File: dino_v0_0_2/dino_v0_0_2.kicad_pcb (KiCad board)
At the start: 4 copper layers, 298.9 x 270 mm, 207 parts, among them J1 DINO_BUS_SOCKET, J10 PS_ON, J11 Conn_01x08_Socket, J2 DINO_BUS_SOCKET, J3 DINO_BUS_SOCKET, J4 DINO_BUS_SOCKET, J5 DINO_BUS_SOCKET, J6 DINO_BUS_SOCKET, J7 DINO_BUS_SOCKET, J8 DINO_BUS_SOCKET, J9 ATX-24, SW2 RESET_BTN, U1 74LS193, U10 74LS02, U11 74LS245, U12 74LS245, U13 74LS245, U14 74LS245, U15 AT28C64B, U16 74LS244N, U17 74LS244N, U18 74LS373, U19 74LS245, U2 74LS193, U20 74LS163, U21 74LS245, U22 74LS02, U23 AT28C64B, U24 AT28C256, U25 74LS245, U26 MCM60256AP, U27 74LS74, U28 74LS138, U29 74LS138, U3 74LS193, U30 74LS138, U31 74LS373, U32 74LS373, U33 74LS373, U34 74LS373, U35 74LS373, U36 7400, U37 74LS04, U38 74F382N, U39 74LS00, U4 74LS193, U40 74F382N, U41 74LS245, U42 74LS245, U43 74LS245, U44 74LS245, U45 74LS373, U46 74LS373, U47 74LS373, U48 74LS157, U49 74LS273, U5 74LS08, U50 74LS02, U51 7400, U52 74LS02, U53 74LS08, U54 74LS245, U55 74LS373, U56 74LS14, U57 74LS02, U58 74LS373, U59 74LS245, U6 74LS163, U60 74LS02, U61 74LS02, U62 74LS02, U63 74LS169, U64 74LS169, U65 74LS169, U66 74LS169, U67 74LS245, U68 74LS245, U69 74LS08, U7 74LS138, U70 74LS138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

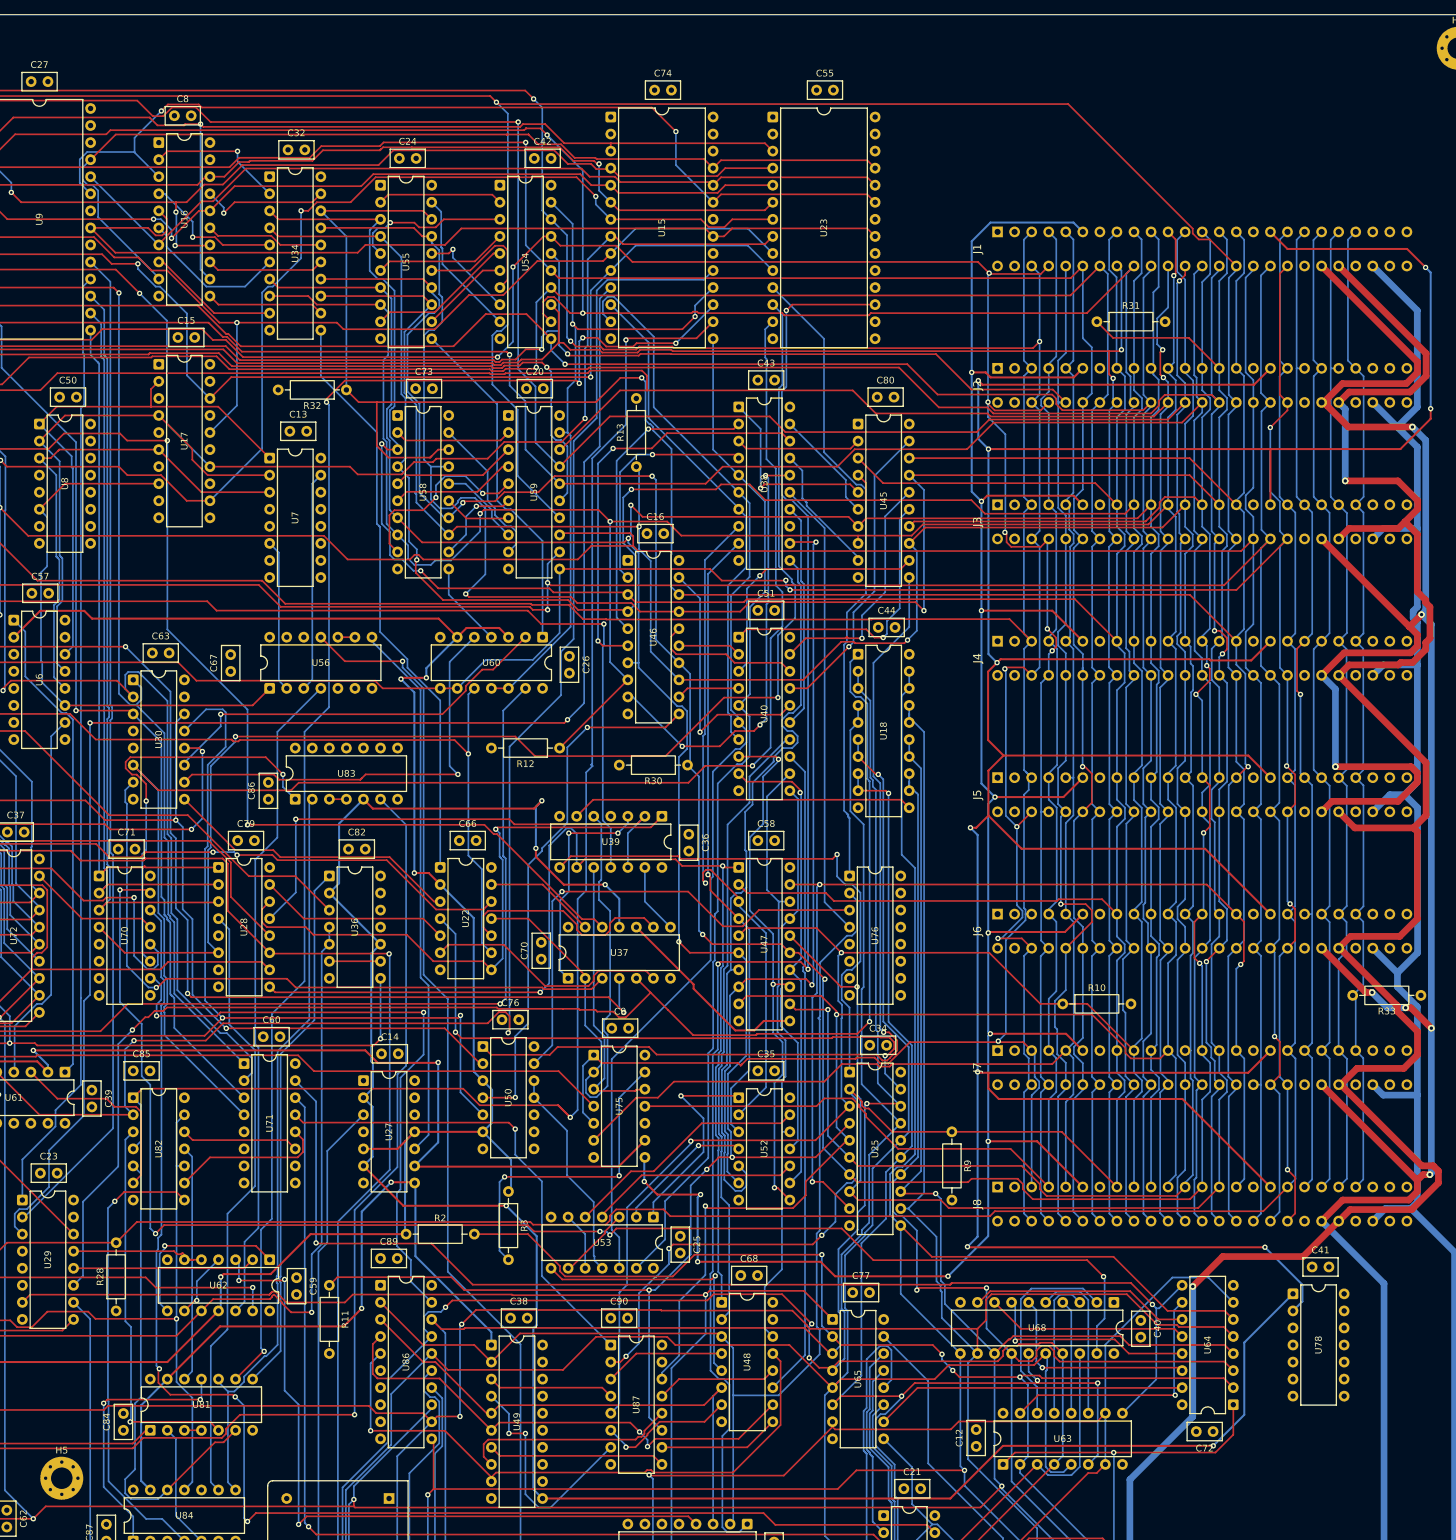
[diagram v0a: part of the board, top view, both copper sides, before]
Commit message: feat(pcb): Hamr logo, Katari board text, Rev A fab package
Silkscreen, upper right: the Hamr logo (logo_sm from the Disk Hamr
project, copied into a new project library dino.pretty as hamr_logo)
and the title / revision / ID block in Katari, laid out as on Disk Hamr.
H5 nudged 0.1 mm off an MDR6 track (clearance 0.178 -> 0.278 mm).

fabrication/: gerbers (F.Cu, In1.Cu GND, In2.Cu +5V, B.Cu, masks, silk,
Edge.Cuts), PTH/NPTH Excellon drills with maps, and the zip uploaded
to PCBWay.

KiCad DRC: 0 unconnected, 0 errors, parity 0; one warning, the ID
block's TrueType strokes are thin (not bold).

Co-Authored-By: Claude Opus 5.5 <noreply@anthropic.com>
Claude-Session: https://claude.ai/code/session_01JGxSS4MVUcaZdKZGtKroSg
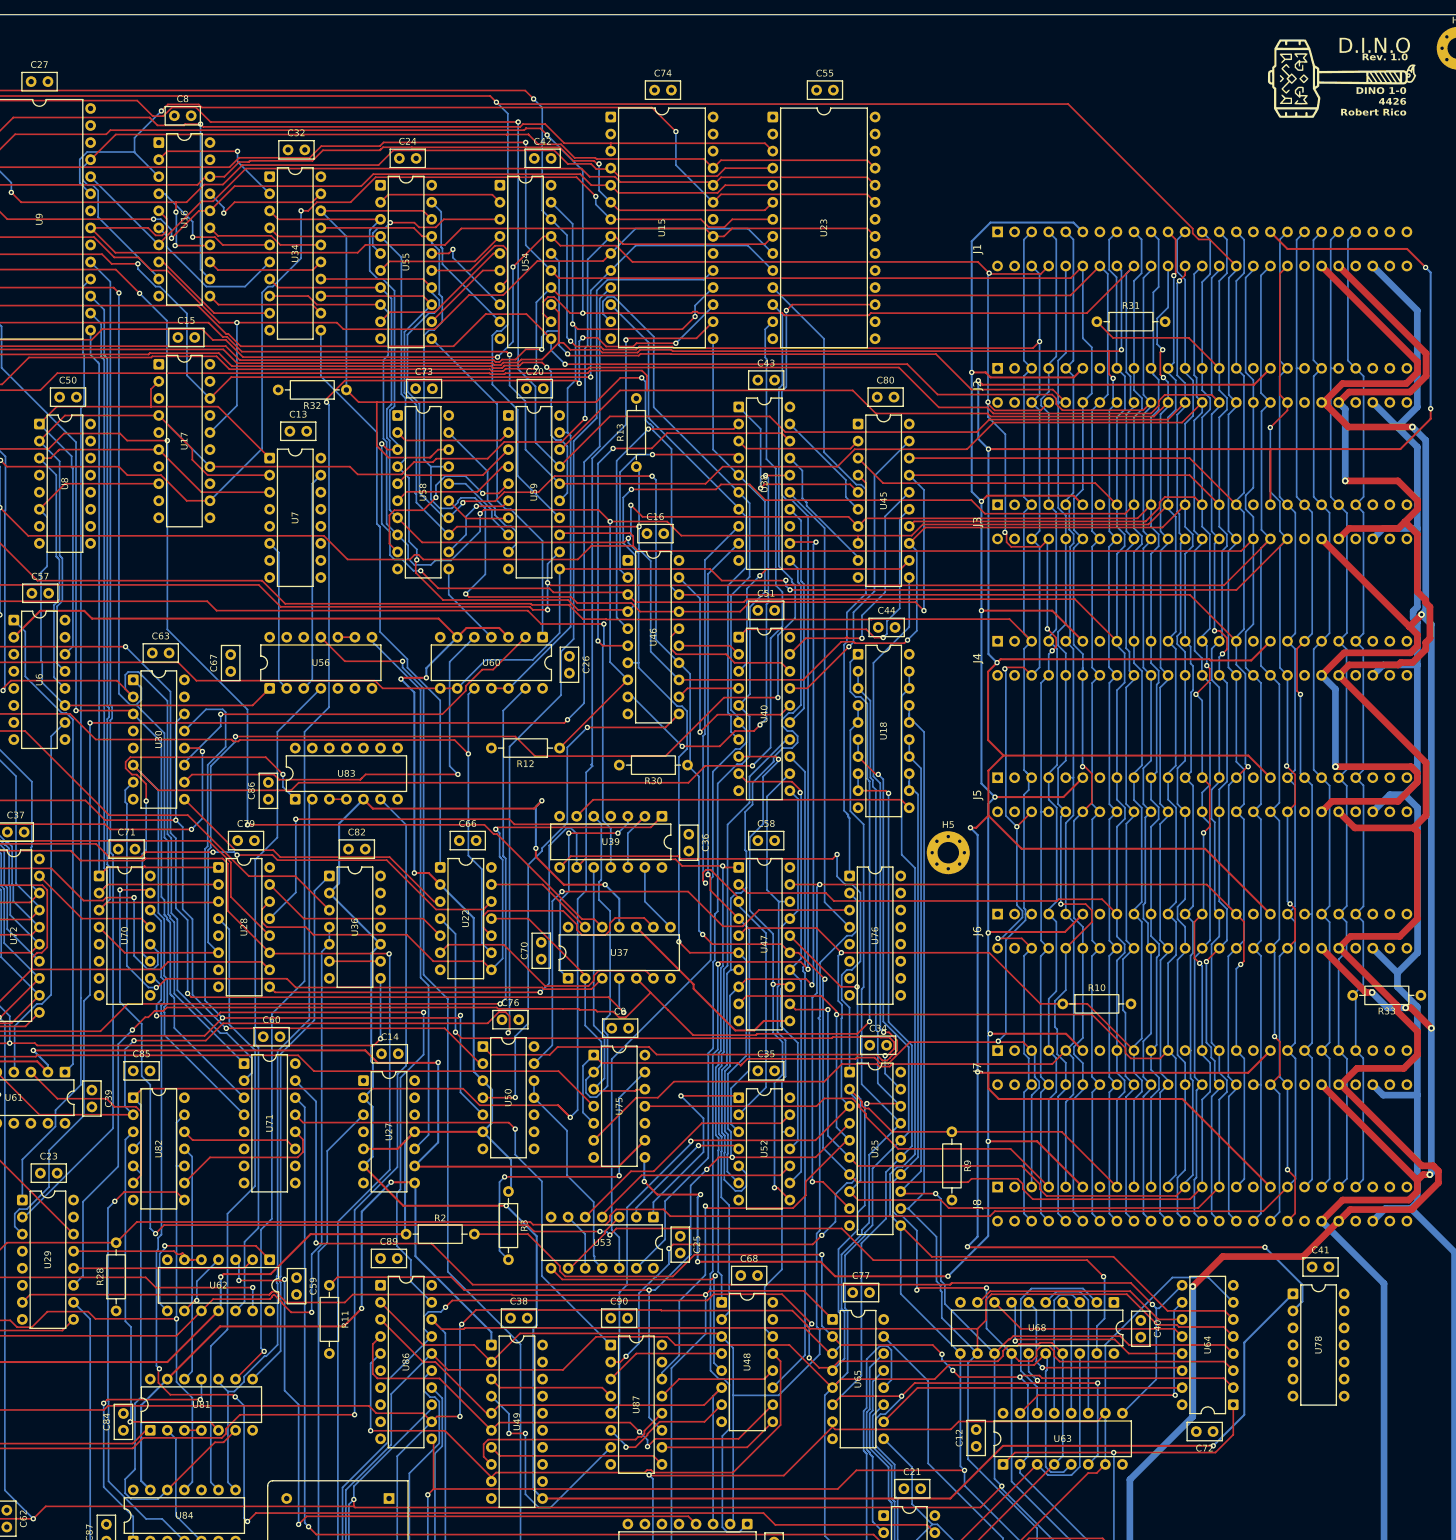
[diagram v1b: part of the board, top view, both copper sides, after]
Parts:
- added G1: LOGO, dino:hamr_logo, F.Cu at (276.5, 9.50)
- moved H5 161.6 mm to (217.9, 124.8)
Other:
- board text added: "D.I.N.O"
- board text added: "DINO 1-0 4426 Robert Rico"
- board text added: "Rev. 1.0"
